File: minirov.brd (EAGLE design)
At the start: 50.8 x 50.8 mm, 69 parts, among them Q1 DMN6140L-13DICT-ND, Q2 DMN6140L-13DICT-ND, U1 DRV8848PWP, U2 DRV8848PWP, Y1 ECS-80-S-4X

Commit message: first iteration of schematic and board placements
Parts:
- removed C1, C10, C2, C3, C4, C5, C6, C7, C8, C9: 4.7uF, SparkFun-Capacitors:0603
- removed C11: 0.1uF, SparkFun-Capacitors:0603
- removed R1, R10, R11, R2, R3: 1k, SparkFun-Resistors:0603
- removed RESET: (no value), DiscreteComponents:SW_2512
- removed SV1: (no value), con-lsta:FE05-1
- removed Y1: ECS-80-S-4X, ECS-80-S-4X:XTAL_ECS-80-S-4X
- added C19: 100nF, SparkFun-Capacitors:0603
- added J21: (no value), SparkFun-Connectors:1X01
- added U$8: TLE493DW2B6, TLE493DW2B6:TLE493DW2B6
- added U$9: RPI-ZERO, RPI-Zero:RASPBERRYPI_BASTELSTUBE_V13_RASPI_BOARD_B+_FULL
- U$2: value TCAN337D -> 74CBTLV3257PW; device PI_Shield_Library:TCAN337D -> 74CBTLV3257PW:74CBTLV3257PW
- moved J10 76.4 mm to (62.2, 10.2)
- moved U$4 58.9 mm to (53.3, 20.8)
- moved U$1 56.4 mm to (-33.5, 24.1)
- moved J13 51.1 mm to (-34.3, 16.5)
- moved J14 49.9 mm to (-30.2, 16.5)
- moved J4 48.6 mm to (27.2, 2.29)
- moved J3 46.9 mm to (24.5, 2.29)
- moved R5 42.7 mm to (28.4, 7.11), flipped to the bottom, turned to 270 degrees
- moved D1 40.9 mm to (-6.35, 22.1)
- moved J15 36.8 mm to (2.79, 20.6), turned to 0 degrees
- moved U2 35.9 mm to (26.4, 8.89), turned to 90 degrees
- moved R6 35.2 mm to (-4.57, 26.4), turned to 270 degrees
- moved U$3 32.5 mm to (43.2, 20.8)
- moved C17 31.2 mm to (28.4, 10.7), flipped to the bottom, turned to 90 degrees
- moved J11 31.0 mm to (8.64, 17.0), flipped to the bottom
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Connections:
- removed net N$3: C11.2, R10.1, R11.2
- removed net NRST: C7.1, R2.1, RESET.2, SV1.2, U$1.NRST
- removed net PWM3: U2.16
- removed net PWM4: U2.15
- new net MTR1_PWM: U$2.1A, U$9.33
- new net MTR2_PWM: U$2.2A, U$9.12
- new net MTR_AB_SEL: U$2.S, U$9.16
- new net MTR_NOE: U$2.NOE, U$9.15
- net +3V3: now also C19.2, J21.1, U$2.3V3, U$8.3V3; no longer C1.1, C10.1, C2.1, C3.1, C4.1, C5.1, C6.1, R2.2, SV1.5, U$1.VDD, U$1.VDDA, U$1.VDDIO2, U$2.VCC
- net +5V: now also U$9.2, U$9.4
- net CAN_H: no longer R10.2, U$2.CANH
- net CAN_L: no longer R11.1, U$2.CANL
- net CAN_STM_RX: no longer U$2.TXD
- net CAN_STM_TX: no longer U$2.RXD
- net GND: now also C19.1, U$8.GND1, U$8.GND2, U$8.GND3, U$9.14, U$9.20, U$9.25, U$9.30, U$9.34, U$9.39, U$9.6, U$9.9; no longer C1.2, C10.2, C11.1, C2.2, C3.2, C4.2, C5.2, C6.2, C7.2, C8.2, C9.2, RESET.1, SV1.1
- net LED1_PWM: now also U$9.11; no longer U$1.PA6
- net LED2_PWM: now also U$9.13; no longer U$1.PA7
- net MISO: now also U$9.21; no longer U$1.PB4
- net MOSI: now also U$9.19; no longer U$1.PB5
- net MTR_1A_PWM: now also U$2.1B1; no longer U$1.PA0
- net MTR_1B_PWM: now also U$2.1B2; no longer U$1.PA1
- net MTR_2A_PWM: now also U$2.2B1, U2.16; no longer U$1.PA2
- net MTR_2B_PWM: now also U$2.2B2, U2.15; no longer U$1.PA3
- net N$1: now also U$9.8; no longer C9.1, R1.1, Y1.2
- net N$2: now also U$9.10; no longer C8.1, R3.1, Y1.1
- net OSC_IN: no longer R3.2
- net OSC_OUT: no longer R1.2
- net SCK: now also U$9.23; no longer U$1.PB3
- net SCL: now also U$8.SCL, U$9.5; no longer U$1.PB6
- net SDA: now also U$8.SDA, U$9.3; no longer U$1.PB7
- net SWCLK: no longer SV1.3
- net SWDIO: no longer SV1.4
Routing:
- added copper zone on layer 1, net GND
- added copper zone on layer 16, net GND
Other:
- board size 50.8 x 50.8 mm -> 65.8 x 30.7 mm

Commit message: minor changes
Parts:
- moved J15 2.54 mm to (5.33, 20.4), turned to 180 degrees
- moved U$9 0.57 mm to (1.52, 34.3)
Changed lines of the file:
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@@
 <setting verticaltext="up"/>
 </settings>
-<grid distance="10" unitdist="mil" unit="mil" style="lines" multiple="1" display="no" altdistance="5" altunitdist="mil" altunit="mil"/>
+<grid distance="5" unitdist="mil" unit="mil" style="lines" multiple="1" display="no" altdistance="5" altunitdist="mil" altunit="mil"/>
 <layers>
 <layer number="1" name="Top" color="4" fill="1" visible="yes" active="yes"/>
@@
 <element name="J13" library="SparkFun-Connectors" library_urn="urn:adsk.eagle:library:513" package="1X01" package3d_urn="urn:adsk.eagle:package:38028/1" value="" x="-34.29" y="16.51"/>
 <element name="J14" library="SparkFun-Connectors" library_urn="urn:adsk.eagle:library:513" package="1X01" package3d_urn="urn:adsk.eagle:package:38028/1" value="" x="-30.226" y="16.51"/>
-<element name="J15" library="SparkFun-Connectors" library_urn="urn:adsk.eagle:library:513" package="1X02" package3d_urn="urn:adsk.eagle:package:38039/1" value="" x="2.794" y="20.574"/>
+<element name="J15" library="SparkFun-Connectors" library_urn="urn:adsk.eagle:library:513" package="1X02" package3d_urn="urn:adsk.eagle:package:38039/1" value="" x="5.334" y="20.447" rot="R180"/>
 <element name="D1" library="SparkFun-LED" library_urn="urn:adsk.eagle:library:529" package="LED-0603" package3d_urn="urn:adsk.eagle:package:39354/1" value="" x="-6.35" y="22.098"/>
 <element name="Q1" library="minirov" package="SOT23-3" value="DMN6140L-13DICT-ND" x="9.398" y="9.398" rot="R180"/>
@@
 <attribute name="PROD_ID" value="CAP-00867" x="4.064" y="12.192" size="1.778" layer="27" display="off"/>
 </element>
-<element name="U$9" library="RPI-Zero" package="RASPBERRYPI_BASTELSTUBE_V13_RASPI_BOARD_B+_FULL" value="RPI-ZERO" x="1.016" y="34.544"/>
+<element name="U$9" library="RPI-Zero" package="RASPBERRYPI_BASTELSTUBE_V13_RASPI_BOARD_B+_FULL" value="RPI-ZERO" x="1.524" y="34.29"/>
 <element name="U$2" library="74CBTLV3257PW" package="74CBTLV3257PW" value="74CBTLV3257PW" x="23.114" y="17.78"/>
 <element name="J21" library="SparkFun-Connectors" library_urn="urn:adsk.eagle:library:513" package="1X01" package3d_urn="urn:adsk.eagle:package:38028/1" value="" x="5.08" y="17.018"/>
@@
 <contactref element="U$9" pad="34"/>
 <contactref element="U$2" pad="GND"/>
-<wire x1="50.026" y1="62.314" x2="57.646" y2="59.774" width="0" layer="19" extent="1-1"/>
-<wire x1="44.946" y1="62.314" x2="50.026" y2="62.314" width="0" layer="19" extent="1-1"/>
-<wire x1="39.866" y1="59.774" x2="44.946" y2="62.314" width="0" layer="19" extent="1-1"/>
-<wire x1="32.246" y1="62.314" x2="39.866" y2="59.774" width="0" layer="19" extent="1-1"/>
-<wire x1="24.626" y1="62.314" x2="32.246" y2="62.314" width="0" layer="19" extent="1-1"/>
-<wire x1="19.546" y1="59.774" x2="24.626" y2="62.314" width="0" layer="19" extent="1-1"/>
-<wire x1="14.466" y1="62.314" x2="19.546" y2="59.774" width="0" layer="19" extent="1-1"/>
-<wire x1="43.18" y1="20.828" x2="39.866" y2="59.774" width="0" layer="19" extent="1-1"/>
-<wire x1="-5.473" y1="22.098" x2="2.032" y2="17.018" width="0" layer="19" extent="1-1"/>
+<wire x1="2.032" y1="17.018" x2="-5.473" y2="22.098" width="0" layer="19" extent="1-1"/>
 <wire x1="-26.478" y1="22.68" x2="-5.473" y2="22.098" width="0" layer="19" extent="1-1"/>
 <wire x1="-31.278" y1="31.18" x2="-26.478" y2="22.68" width="0" layer="19" extent="1-1"/>
@@
 <contactref element="U$8" pad="SDA"/>
 <contactref element="U$9" pad="3"/>
-<wire x1="5.334" y1="20.574" x2="11.926" y2="59.774" width="0" layer="19" extent="1-1"/>
-<wire x1="2.606" y1="10.723" x2="5.334" y2="20.574" width="0" layer="19" extent="1-1"/>
+<wire x1="2.794" y1="20.447" x2="12.434" y2="59.52" width="0" layer="19" extent="1-1"/>
+<wire x1="2.606" y1="10.723" x2="2.794" y2="20.447" width="0" layer="19" extent="1-1"/>
 </signal>
 <signal name="SCL">
@@
 <contactref element="U$8" pad="SCL"/>
 <contactref element="U$9" pad="5"/>
-<wire x1="2.794" y1="20.574" x2="14.466" y2="59.774" width="0" layer="19" extent="1-1"/>
-<wire x1="2.606" y1="8.073" x2="2.794" y2="20.574" width="0" layer="19" extent="1-1"/>
+<wire x1="5.334" y1="20.447" x2="14.974" y2="59.52" width="0" layer="19" extent="1-1"/>
+<wire x1="2.606" y1="8.073" x2="5.334" y2="20.447" width="0" layer="19" extent="1-1"/>
 </signal>
 <signal name="USART_RX">
@@
 <contactref element="Q1" pad="1"/>
 <contactref element="U$9" pad="11"/>
-<wire x1="10.348" y1="10.398" x2="22.086" y2="59.774" width="0" layer="19" extent="1-1"/>
+<wire x1="10.348" y1="10.398" x2="22.594" y2="59.52" width="0" layer="19" extent="1-1"/>
 </signal>
 <signal name="LED2_PWM">
 <contactref element="Q2" pad="1"/>
 <contactref element="U$9" pad="13"/>
-<wire x1="14.666" y1="10.398" x2="24.626" y2="59.774" width="0" layer="19" extent="1-1"/>
+<wire x1="14.666" y1="10.398" x2="25.134" y2="59.52" width="0" layer="19" extent="1-1"/>
 </signal>
 <signal name="MOSI">
@@
 <contactref element="U$9" pad="4"/>
 <wire x1="62.23" y1="10.16" x2="50.8" y2="20.828" width="0" layer="19" extent="1-1"/>
-<wire x1="8.636" y1="17.018" x2="50.8" y2="20.828" width="0" layer="19" extent="1-1"/>
-<wire x1="9.386" y1="62.314" x2="8.636" y2="17.018" width="0" layer="19" extent="1-1"/>
-<wire x1="11.926" y1="62.314" x2="9.386" y2="62.314" width="0" layer="19" extent="1-1"/>
+<wire x1="12.434" y1="62.06" x2="50.8" y2="20.828" width="0" layer="19" extent="1-1"/>
+<wire x1="9.894" y1="62.06" x2="12.434" y2="62.06" width="0" layer="19" extent="1-1"/>
+<wire x1="8.636" y1="17.018" x2="9.894" y2="62.06" width="0" layer="19" extent="1-1"/>
 </signal>
 <signal name="N$1">
@@
 <contactref element="U$2" pad="S"/>
 <contactref element="U$9" pad="16"/>
-<wire x1="20.839" y1="14.78" x2="27.166" y2="62.314" width="0" layer="19" extent="1-1"/>
+<wire x1="20.839" y1="14.78" x2="27.674" y2="62.06" width="0" layer="19" extent="1-1"/>
 </signal>
 <signal name="MTR2_PWM">
 <contactref element="U$9" pad="12"/>
 <contactref element="U$2" pad="2A"/>
-<wire x1="24.739" y1="14.78" x2="22.086" y2="62.314" width="0" layer="19" extent="1-1"/>
+<wire x1="24.739" y1="14.78" x2="22.594" y2="62.06" width="0" layer="19" extent="1-1"/>
 </signal>
 <signal name="MTR1_PWM">
 <contactref element="U$9" pad="33"/>
 <contactref element="U$2" pad="1A"/>
-<wire x1="22.789" y1="14.78" x2="50.026" y2="59.774" width="0" layer="19" extent="1-1"/>
+<wire x1="22.789" y1="14.78" x2="50.534" y2="59.52" width="0" layer="19" extent="1-1"/>
 </signal>
 <signal name="MTR_NOE">
 <contactref element="U$9" pad="15"/>
 <contactref element="U$2" pad="NOE"/>
-<wire x1="21.489" y1="20.78" x2="27.166" y2="59.774" width="0" layer="19" extent="1-1"/>
+<wire x1="21.489" y1="20.78" x2="27.674" y2="59.52" width="0" layer="19" extent="1-1"/>
 </signal>
 </signals>

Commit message: first round of routing. need to gnd stitch
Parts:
- moved U$1 84.9 mm to (39.8, -18.7), turned to 180 degrees
- moved J13 79.8 mm to (40.6, -11.0), turned to 180 degrees
- moved J14 72.2 mm to (36.5, -11.0), turned to 180 degrees
- moved R6 62.8 mm to (48.5, -7.11), turned to 90 degrees
- moved D1 60.9 mm to (48.7, -3.94), turned to 90 degrees
- moved U$9 34.3 mm to (0.64, 0.00)
- moved J11 7.62 mm to (2.03, 20.8)
- moved C18 3.67 mm to (36.4, 11.9), turned to 270 degrees
- moved C12 2.75 mm to (17.8, 13.1), turned to 0 degrees
- moved J15 2.29 mm to (4.57, 18.3)
- moved R8 2.19 mm to (35.7, 14.3)
- moved C15 2.02 mm to (23.4, 12.4), turned to 90 degrees
- moved U$5 1.84 mm to (36.3, 16.6)
- moved R4 1.73 mm to (21.8, 5.40)
- moved U1 1.73 mm to (19.7, 7.18)
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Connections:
- removed net 12V: U$4.VIN
- net +12V: now also U$4.VIN
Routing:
- net +3V3: track 0.00 -> 123.8 mm, vias 0 -> 6
- net +5V: track 0.00 -> 91.6 mm
- net +12V: track 0.00 -> 84.6 mm, vias 0 -> 3
- net MTR1_PWM: track 0.00 -> 31.5 mm
- net SCL: track 0.00 -> 29.7 mm
- net MTR2_PWM: track 0.00 -> 27.1 mm, vias 0 -> 2
- net SDA: track 0.00 -> 21.3 mm
- net LED1_PWM: track 0.00 -> 21.0 mm
- net LED2_PWM: track 0.00 -> 21.0 mm
- net MTR_AB_SEL: track 0.00 -> 16.8 mm, vias 0 -> 2
- net USART_TX: track 0.00 -> 16.0 mm
- net RS-OUT: track 0.00 -> 13.5 mm, vias 0 -> 2
- net RS-IN: track 0.00 -> 8.34 mm
- net MTR_1A_PWM: track 0.00 -> 8.31 mm
- net MTR_1B_PWM: track 0.00 -> 8.31 mm
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
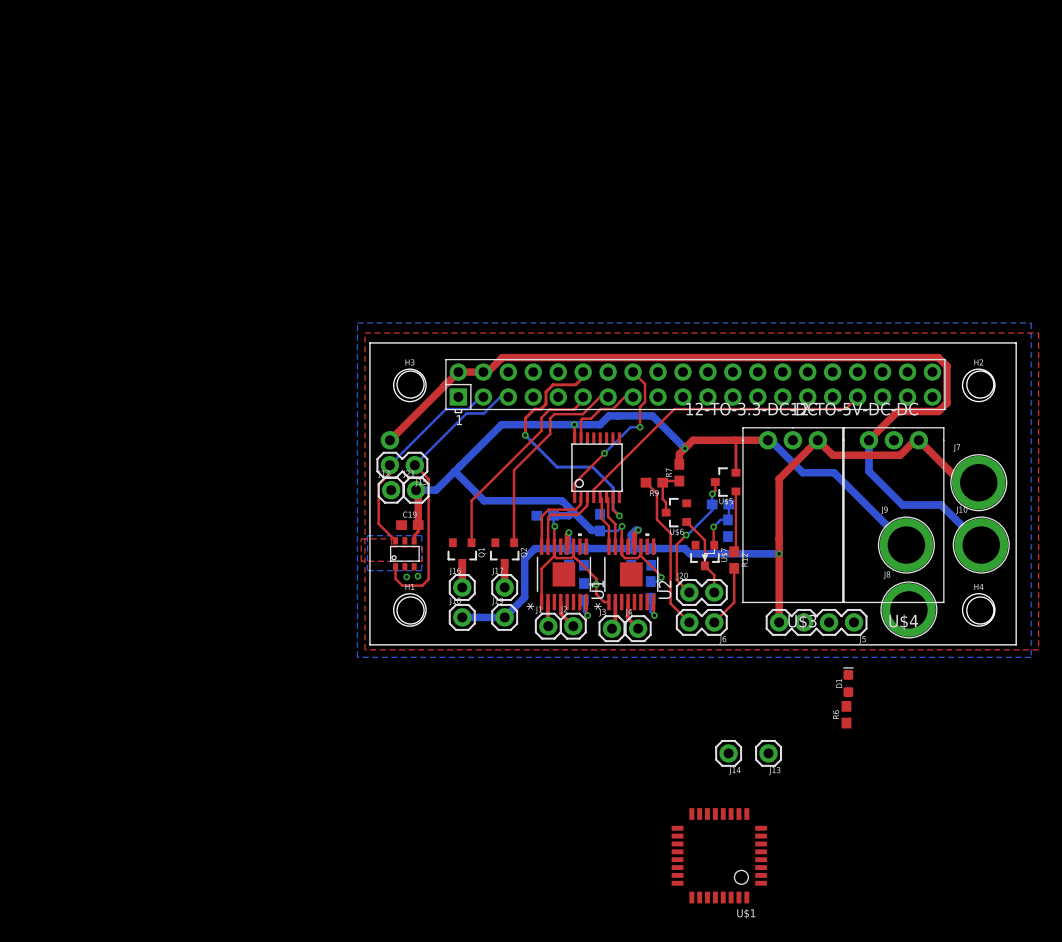
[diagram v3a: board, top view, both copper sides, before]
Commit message: added ADC
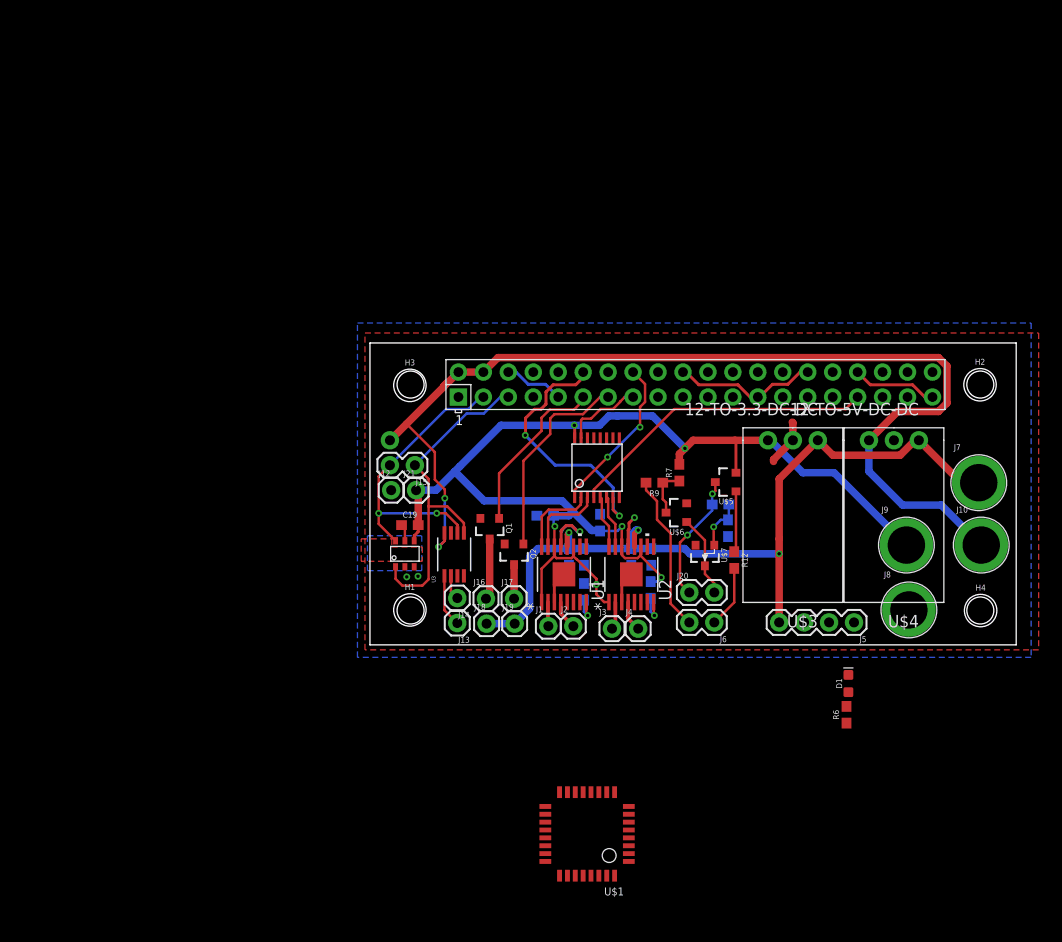
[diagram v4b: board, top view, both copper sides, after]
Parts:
- added U3: MAX1136EUA-T, MAX1136EUA-T:21-0036K
- moved J13 34.4 mm to (8.89, 2.22)
- moved J14 31.8 mm to (8.89, 4.76)
- moved U$1 13.6 mm to (26.4, -16.4)
- moved Q1 3.73 mm to (12.2, 11.9)
- moved J16 2.67 mm to (11.8, 4.70)
- moved J18 2.56 mm to (11.9, 2.16)
- moved J17 1.49 mm to (14.7, 4.70)
- moved J19 1.20 mm to (14.7, 2.16)
- moved Q2 0.96 mm to (14.7, 9.27)
- moved H4 0.20 mm to (62.2, 3.49)
- moved H2 0.14 mm to (62.1, 26.5)
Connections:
- net +5V: now also U3.8
- net ADC_IN1: now also U3.1; no longer U$1.PA4
- net ADC_IN2: now also U3.2; no longer U$1.PA5
- net GND: now also U3.7
- net SCL: now also U3.5
- net SDA: now also U3.6
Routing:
- net GND: track 0.00 -> 52.4 mm, vias 2 -> 4
- net +5V: track 91.6 -> 107.6 mm, vias 0 -> 2
- net SDA: track 21.3 -> 30.6 mm, vias 0 -> 2
- net ADC_IN1: track 0.00 -> 5.34 mm
- net SCL: track 29.7 -> 35.0 mm
- net N$7: track 2.46 -> 6.23 mm
- net LED1_PWM: track 21.0 -> 17.4 mm
- net ADC_IN2: track 0.00 -> 2.53 mm
- net +12V: track 84.6 -> 83.2 mm
- net N$6: track 2.46 -> 3.47 mm
